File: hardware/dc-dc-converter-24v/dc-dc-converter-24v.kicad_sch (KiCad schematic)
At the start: 49 parts, among them IC1 LM5122MHX_NOPB, J1 12V, J2 24V, Q1 SQJA42EP, Q2 SQJA42EP

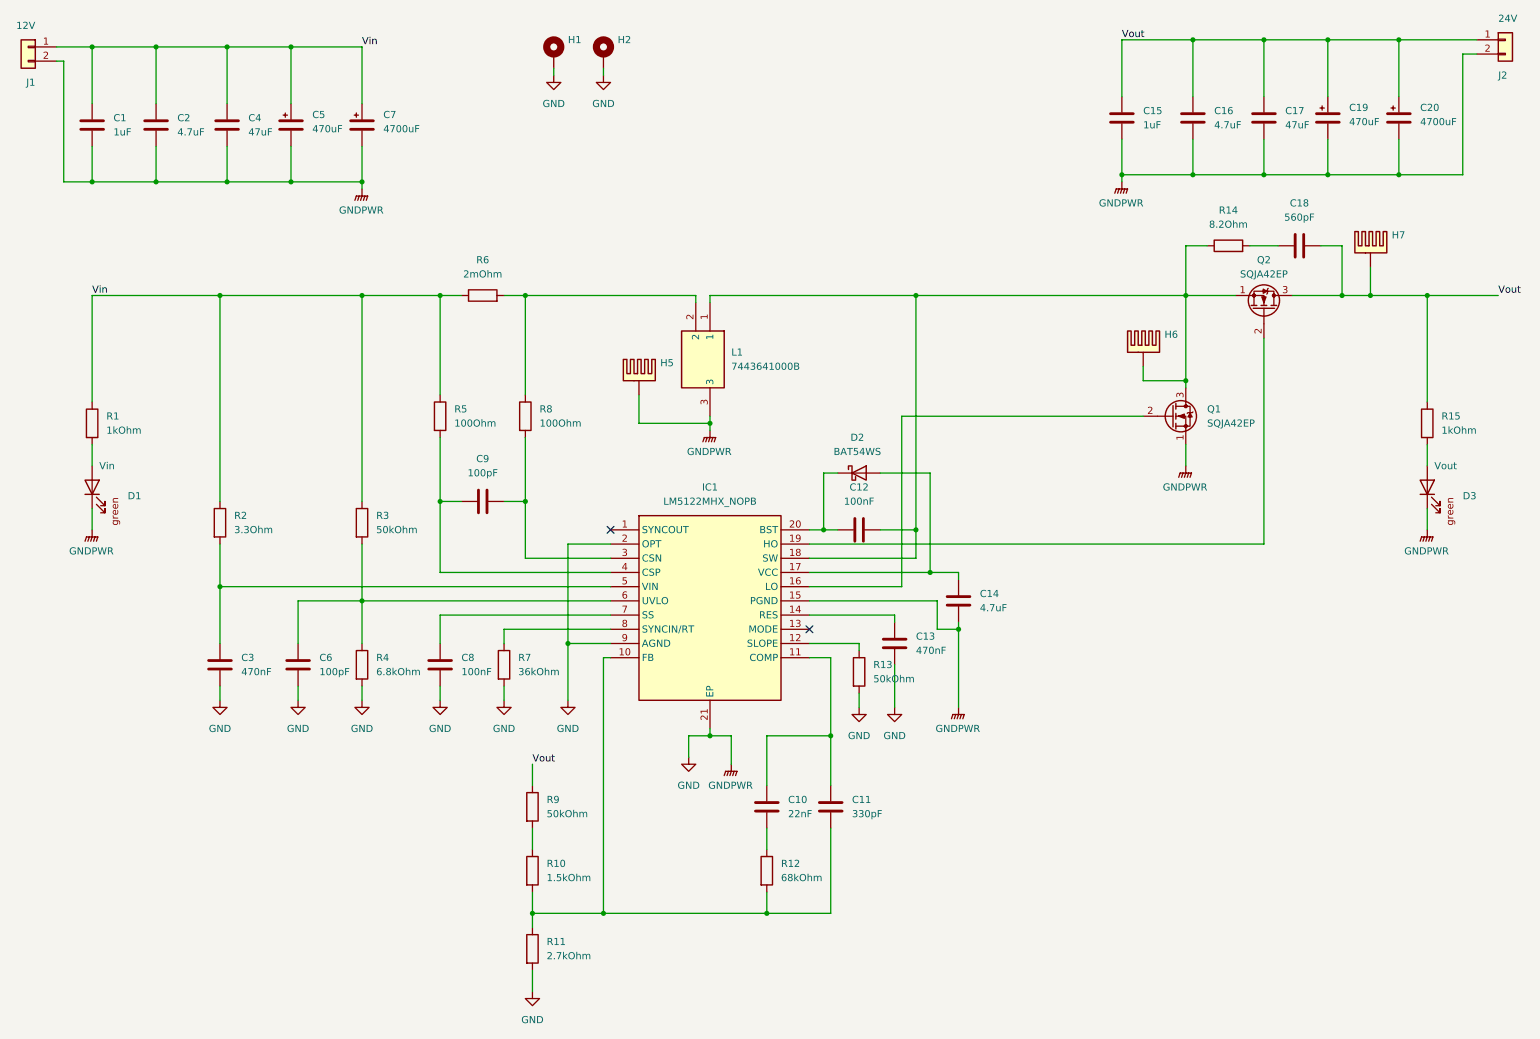
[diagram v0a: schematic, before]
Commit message: change type of heatsinks
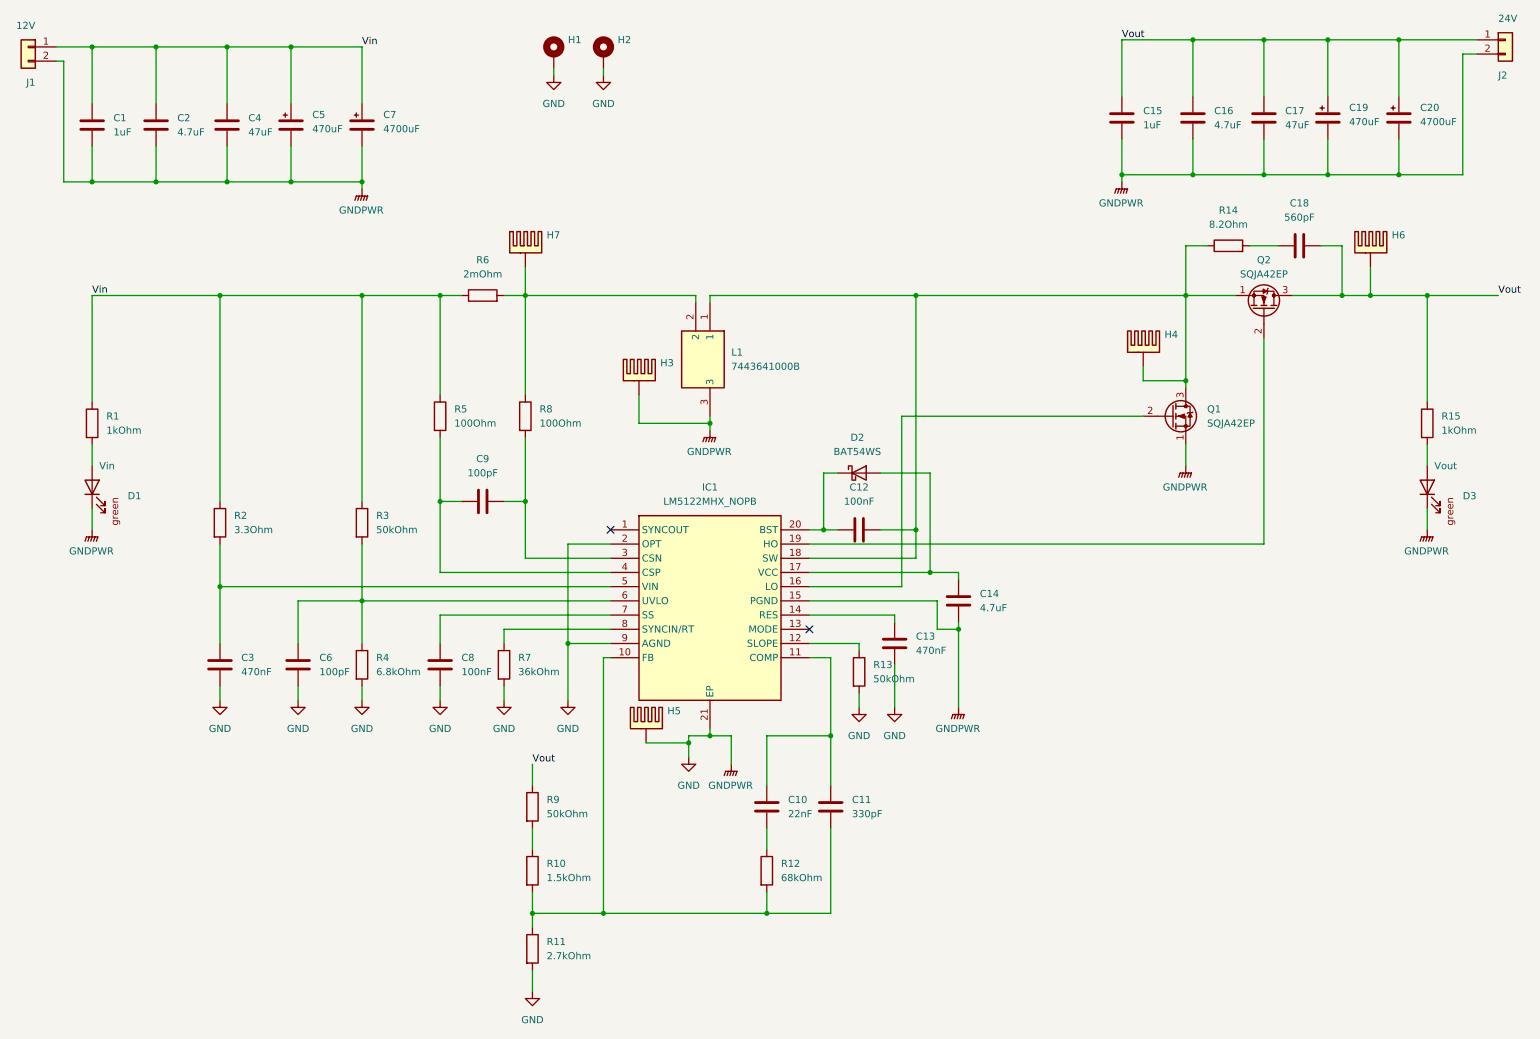
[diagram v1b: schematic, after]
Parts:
- removed H5, H6, H7: heatsink_HSB43-454515P, benediktibk:HSB43-454515P, symbol benediktibk:heatsink_HSB43-454515P
- added H3, H4, H5, H6, H7: ~, benediktibk:heatsink_18x18, symbol benediktibk:heatsink_18x18
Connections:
- net GND: now also H3.PAD, H5.PAD
- net Vout: now also H6.PAD
- net at C12.2, IC1.18 (SW), L1.1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: now also H4.PAD
- net at L1.2, R6.2, R8.1: now also H7.PAD

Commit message: update symbols and footprints
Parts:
- C1, C15: Mouser Part Number (none) -> 963-UMK107BJ105KA-T
- C10: Mouser Part Number 80-C0603C223K4RAC -> 80-C0603C223K4RAC
- C12, C8: Mouser Part Number (none) -> 581-KGM15BR71H104KM
- C14, C16, C2: Mouser Part Number (none) -> 187-CL21A475KBQNNNE
- C17, C4: Mouser Part Number (none) -> 810-C3216X5R1E476M
- C19, C5: Mouser Part Number (none) -> 647-UCD1J471MNQ1MS
- C20, C7: Mouser Part Number (none) -> 80-ESK478M050AQ3AA
- D1, D3: Mouser Part Number (none) -> 604-AP1608SGC
- D2: Mouser Part Number (none) -> 637-BAT54WS
- H3, H4, H5, H6, H7: Mouser Part Number (none) -> 490-HSB06-181810
- R12: Mouser Part Number (none) -> 603-RT0603FRE0768KL
- R5, R8: Mouser Part Number (none) -> 279-CRGH0603F100R
- R6: Mouser Part Number (none) -> 660-TLR3APSDTE2L00F7
- R7: Mouser Part Number (none) -> 652-CR0603FX-3602ELF

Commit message: update symbols
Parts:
- C18: Mouser Part Number (none) -> 77-VJ0603A561JXAAC
- Q1, Q2: Mouser Part Number (none) -> 78-SQJA42EP-T1_GE3
- R1, R15: Mouser Part Number (none) -> 603-RC0603FR-101KL
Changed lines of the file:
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@@
 			)
 		)
+		(property "Mouser Part Number" "603-RC0603FR-101KL"
+			(at 10.16 85.09 0)
+			(effects
+				(font
+					(size 1.27 1.27)
+				)
+				(hide yes)
+			)
+		)
 		(pin "1"
 		)
@@
 			)
 		)
+		(property "Mouser Part Number" "77-VJ0603A561JXAAC"
+			(at 242.57 37.084 0)
+			(effects
+				(font
+					(size 1.27 1.27)
+				)
+				(hide yes)
+			)
+		)
 		(pin "1"
 		)
@@
 			)
 		)
+		(property "Mouser Part Number" "78-SQJA42EP-T1_GE3"
+			(at 232.41 68.58 0)
+			(effects
+				(font
+					(size 1.27 1.27)
+				)
+				(hide yes)
+			)
+		)
 		(pin "1"
 		)
@@
 			)
 		)
+		(property "Mouser Part Number" "78-SQJA42EP-T1_GE3"
+			(at 218.44 90.17 0)
+			(effects
+				(font
+					(size 1.27 1.27)
+				)
+				(hide yes)
+			)
+		)
 		(pin "1"
 		)
@@
 			(at 248.92 85.09 0)
 			(effects
+				(font
+					(size 1.27 1.27)
+				)
+				(hide yes)
+			)
+		)
+		(property "Mouser Part Number" "603-RC0603FR-101KL"
+			(at 248.92 85.09 0)
+			(effects

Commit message: generate BOMs
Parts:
- C10: Mouser Part Number 80-C0603C223K4RAC -> 80-C0603C223K4R
- C6, C9: Mouser Part Number 80-C0603C101K5GAC -> 80-C0603C101K5GACLR
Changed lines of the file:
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@@
 			)
 		)
-		(property "Mouser Part Number" "80-C0603C223K4RAC"
+		(property "Mouser Part Number" "80-C0603C223K4R"
 			(at 166.116 153.67 0)
 			(effects
@@
 			)
 		)
-		(property "Mouser Part Number" "80-C0603C101K5GAC"
+		(property "Mouser Part Number" "80-C0603C101K5GACLR"
 			(at 82.296 128.27 0)
 			(effects
@@
 			)
 		)
-		(property "Mouser Part Number" "80-C0603C101K5GAC"
+		(property "Mouser Part Number" "80-C0603C101K5GACLR"
 			(at 96.52 82.804 0)
 			(effects
